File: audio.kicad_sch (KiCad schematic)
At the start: 15 parts, among them SW1 SW_DPST

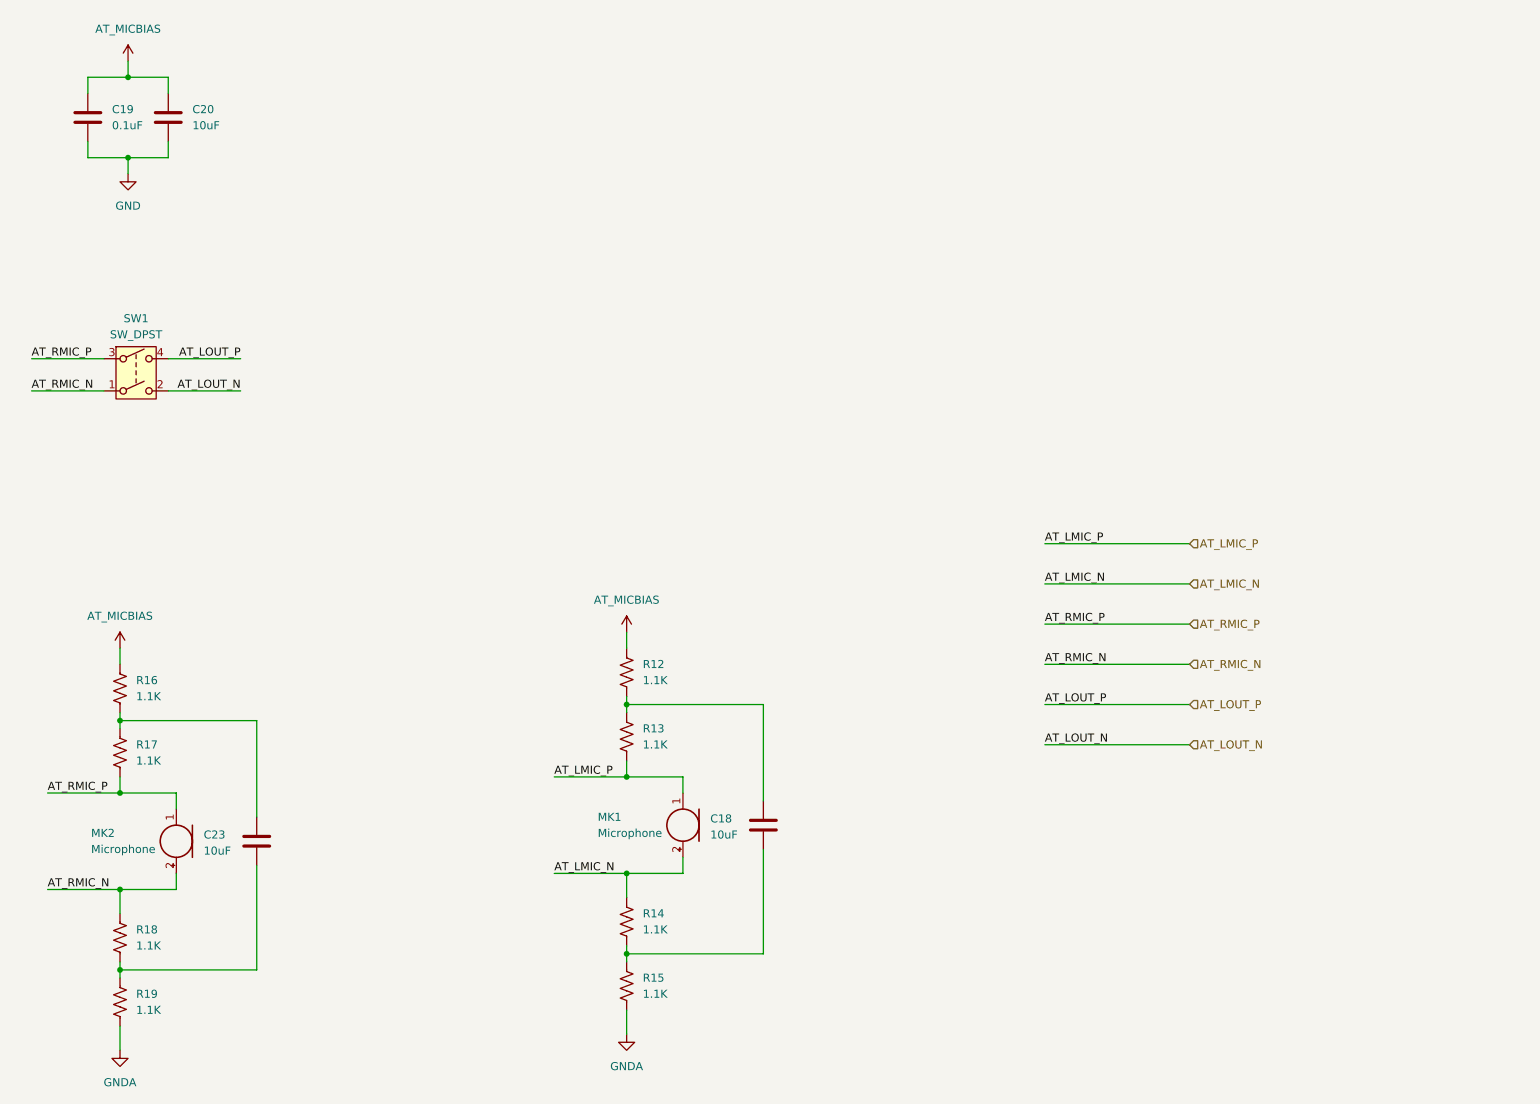
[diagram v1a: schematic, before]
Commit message: fix at820 sym, impl audio pa
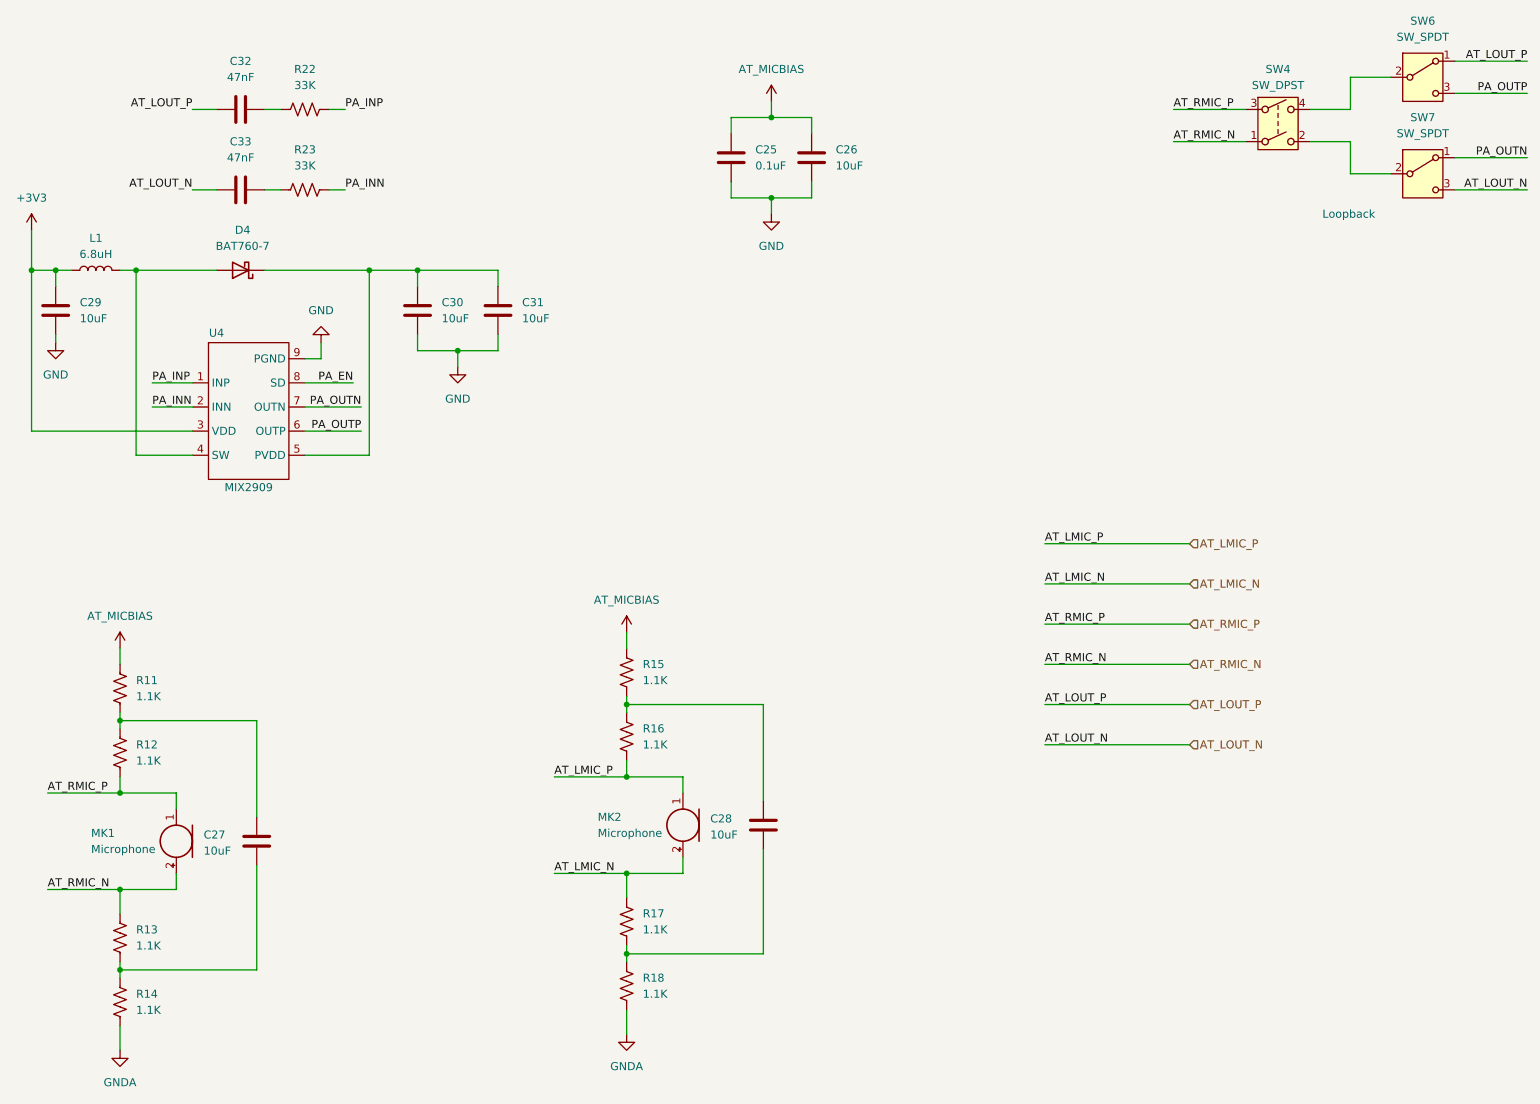
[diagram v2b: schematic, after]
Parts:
- added C29, C30, C31: 10uF, symbol Device:C
- added C32, C33: 47nF, symbol Device:C
- added D4: BAT760-7, Diode_SMD:D_SOD-323, symbol Diode:BAT60A
- added L1: 6.8uH, symbol Device:L
- added R22, R23: 33K, symbol Device:R_US
- added SW6, SW7: SW_SPDT, Button_Switch_SMD:Nidec_Copal_CAS-120A, symbol Switch:SW_SPDT
- added U4: MIX2909, Package_SO:SOIC-8-1EP_3.9x4.9mm_P1.27mm_EP2.29x3mm_ThermalVias, symbol audio:MIX2909
- renumbered C19 to C25, C20 to C26, C23 to C27, C18 to C28, MK2 to MK1, MK1 to MK2, R16 to R11, R17 to R12, R18 to R13, R19 to R14, R12 to R15, R13 to R16, R14 to R17, R15 to R18, SW1 to SW4
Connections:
- net AT_LOUT_N: now also C33.1, SW7.3 (C); no longer SW4.2
- net AT_LOUT_P: now also C32.1, SW6.1 (A); no longer SW4.4
- net GND: now also C29.2, C30.2, C31.2, U4.9 (PGND)
- new net: D4.2 (A), L1.2, U4.4 (SW)
- new net: C32.2, R22.1
- new net: C30.1, C31.1, D4.1 (K), U4.5 (PVDD)
- new net: SW4.2, SW7.2 (B)
- new net: SW4.4, SW6.2 (B)
- new net: C33.2, R23.1
- new net +3V3: C29.1, L1.1, U4.3 (VDD)
- new net PA_EN: U4.8 (SD)
- new net PA_INN: R23.2, U4.2 (INN)
- new net PA_INP: R22.2, U4.1 (INP)
- new net PA_OUTN: SW7.1 (A), U4.7 (OUTN)
- new net PA_OUTP: SW6.3 (C), U4.6 (OUTP)
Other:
- note added: "Loopback"
- moved on the sheet: C25, C26, SW4

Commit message: sch features done, all drc passed
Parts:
- renumbered C29 to C27, C32 to C28, C33 to C29, C27 to C30, C30 to C31, C31 to C32, C25 to C33, C28 to C34, C26 to C35, R11 to R14, R12 to R15, R13 to R16, R14 to R17, R22 to R18, R23 to R19, R15 to R20, R16 to R21, R17 to R22, R18 to R23, SW4 to SW6, SW6 to SW7, SW7 to SW8
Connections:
- net +3V3 renamed +5V

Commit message: asigning footprint
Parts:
- C27, C28, C29, C30, C31, C32, C33, C34, C35: footprint (none) -> Capacitor_SMD:C_0603_1608Metric_Pad1.08x0.95mm_HandSolder
- D4: footprint Diode_SMD:D_SOD-323 -> Diode_SMD:D_SOD-323_HandSoldering
- L1: footprint (none) -> Inductor_SMD:L_0603_1608Metric_Pad1.05x0.95mm_HandSolder
- R14, R15, R16, R17, R18, R19, R20, R21, R22, R23: footprint (none) -> Resistor_SMD:R_0603_1608Metric_Pad0.98x0.95mm_HandSolder
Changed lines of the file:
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@@
 			)
 		)
-		(property "Footprint" ""
+		(property "Footprint" "Capacitor_SMD:C_0603_1608Metric_Pad1.08x0.95mm_HandSolder"
 			(at 141.9352 46.99 0)
 			(hide yes)
@@
 			)
 		)
-		(property "Footprint" ""
+		(property "Footprint" "Capacitor_SMD:C_0603_1608Metric_Pad1.08x0.95mm_HandSolder"
 			(at 35.2552 71.12 0)
 			(hide yes)
@@
 			)
 		)
-		(property "Footprint" ""
+		(property "Footprint" "Resistor_SMD:R_0603_1608Metric_Pad0.98x0.95mm_HandSolder"
 			(at 125.476 174.244 90)
 			(hide yes)
@@
 			)
 		)
-		(property "Footprint" ""
+		(property "Footprint" "Inductor_SMD:L_0603_1608Metric_Pad1.05x0.95mm_HandSolder"
 			(at 40.64 60.96 0)
 			(hide yes)
@@
 			)
 		)
-		(property "Footprint" ""
+		(property "Footprint" "Resistor_SMD:R_0603_1608Metric_Pad0.98x0.95mm_HandSolder"
 			(at 73.914 34.544 90)
 			(hide yes)
@@
 			)
 		)
-		(property "Footprint" ""
+		(property "Footprint" "Capacitor_SMD:C_0603_1608Metric_Pad1.08x0.95mm_HandSolder"
 			(at 92.4052 71.12 0)
 			(hide yes)
@@
 			)
 		)
-		(property "Footprint" ""
+		(property "Footprint" "Resistor_SMD:R_0603_1608Metric_Pad0.98x0.95mm_HandSolder"
 			(at 45.466 176.784 90)
 			(hide yes)
@@
 			)
 		)
-		(property "Footprint" ""
+		(property "Footprint" "Resistor_SMD:R_0603_1608Metric_Pad0.98x0.95mm_HandSolder"
 			(at 45.466 127.254 90)
 			(hide yes)
@@
 			)
 		)
-		(property "Footprint" ""
+		(property "Footprint" "Resistor_SMD:R_0603_1608Metric_Pad0.98x0.95mm_HandSolder"
 			(at 45.466 137.414 90)
 			(hide yes)
@@
 			)
 		)
-		(property "Footprint" "Diode_SMD:D_SOD-323"
+		(property "Footprint" "Diode_SMD:D_SOD-323_HandSoldering"
 			(at 63.5 56.515 0)
 			(hide yes)
@@
 			)
 		)
-		(property "Footprint" ""
+		(property "Footprint" "Capacitor_SMD:C_0603_1608Metric_Pad1.08x0.95mm_HandSolder"
 			(at 145.0848 144.78 0)
 			(hide yes)
@@
 			)
 		)
-		(property "Footprint" ""
+		(property "Footprint" "Resistor_SMD:R_0603_1608Metric_Pad0.98x0.95mm_HandSolder"
 			(at 125.476 124.714 90)
 			(hide yes)
@@
 			)
 		)
-		(property "Footprint" ""
+		(property "Footprint" "Capacitor_SMD:C_0603_1608Metric_Pad1.08x0.95mm_HandSolder"
 			(at 65.0748 147.32 0)
 			(hide yes)
@@
 			)
 		)
-		(property "Footprint" ""
+		(property "Footprint" "Capacitor_SMD:C_0603_1608Metric_Pad1.08x0.95mm_HandSolder"
 			(at 67.31 47.2948 0)
 			(hide yes)
@@
 			)
 		)
-		(property "Footprint" ""
+		(property "Footprint" "Capacitor_SMD:C_0603_1608Metric_Pad1.08x0.95mm_HandSolder"
 			(at 154.6352 46.99 0)
 			(hide yes)
@@
 			)
 		)
-		(property "Footprint" ""
+		(property "Footprint" "Capacitor_SMD:C_0603_1608Metric_Pad1.08x0.95mm_HandSolder"
 			(at 105.1052 71.12 0)
 			(hide yes)
@@
 			)
 		)
-		(property "Footprint" ""
+		(property "Footprint" "Capacitor_SMD:C_0603_1608Metric_Pad1.08x0.95mm_HandSolder"
 			(at 67.31 34.5948 0)
 			(hide yes)
@@
 			)
 		)
-		(property "Footprint" ""
+		(property "Footprint" "Resistor_SMD:R_0603_1608Metric_Pad0.98x0.95mm_HandSolder"
 			(at 125.476 164.084 90)
 			(hide yes)
@@
 			)
 		)
-		(property "Footprint" ""
+		(property "Footprint" "Resistor_SMD:R_0603_1608Metric_Pad0.98x0.95mm_HandSolder"
 			(at 73.914 47.244 90)
 			(hide yes)
@@
 			)
 		)
-		(property "Footprint" ""
+		(property "Footprint" "Resistor_SMD:R_0603_1608Metric_Pad0.98x0.95mm_HandSolder"
 			(at 125.476 134.874 90)
 			(hide yes)
@@
 			)
 		)
-		(property "Footprint" ""
+		(property "Footprint" "Resistor_SMD:R_0603_1608Metric_Pad0.98x0.95mm_HandSolder"
 			(at 45.466 166.624 90)
 			(hide yes)

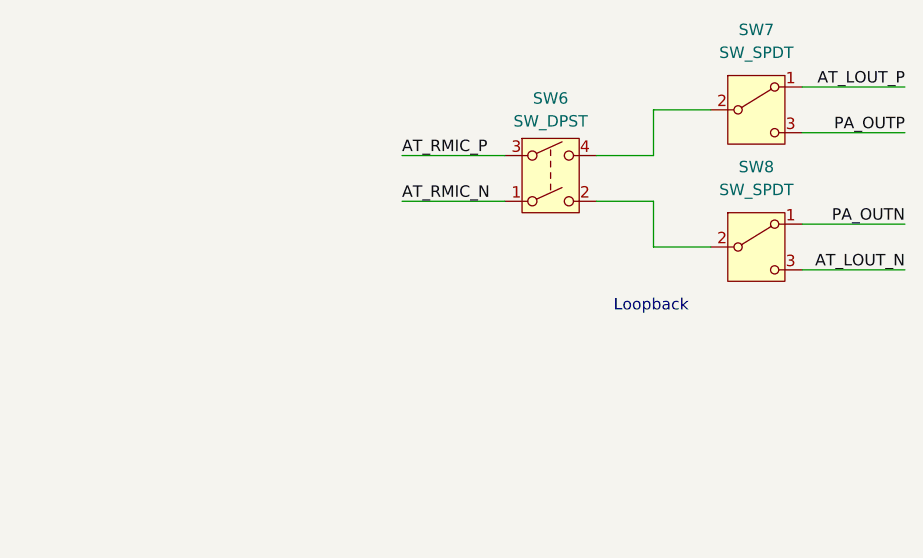
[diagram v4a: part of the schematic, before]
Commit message: refactor some switch circuit
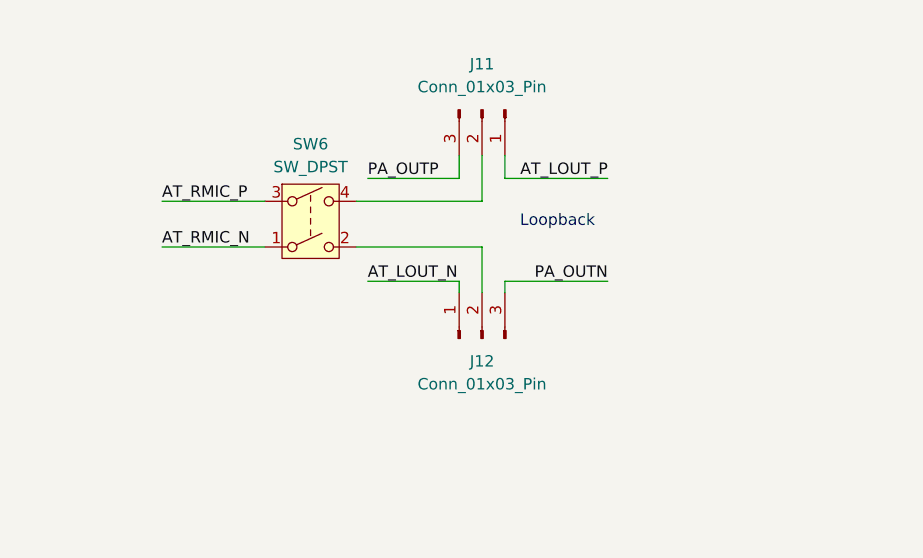
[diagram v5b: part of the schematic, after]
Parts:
- removed SW7, SW8: SW_SPDT, Button_Switch_SMD:Nidec_Copal_CAS-120A, symbol Switch:SW_SPDT
- added J11, J12: Conn_01x03_Pin, Connector_PinHeader_2.54mm:PinHeader_1x03_P2.54mm_Vertical, symbol Connector:Conn_01x03_Pin
- MK1, MK2: footprint (none) -> Capacitor_THT:CP_Radial_D4.0mm_P1.50mm
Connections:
- net AT_LOUT_N: now also J12.1 (Pin_1)
- net AT_LOUT_P: now also J11.1 (Pin_1)
- net PA_OUTN: now also J12.3 (Pin_3)
- net PA_OUTP: now also J11.3 (Pin_3)
- net at SW6.2: now also J12.2 (Pin_2)
- net at SW6.4: now also J11.2 (Pin_2)
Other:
- moved on the sheet: SW6

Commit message: sch all done, footprint done
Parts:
- added LS1: Speaker, Connector_Molex:Molex_PicoBlade_53047-0210_1x02_P1.25mm_Vertical, symbol Device:Speaker
- C28, C29: value 47nF -> 0.1uF
- D4: value BAT760-7 -> SS14; footprint Diode_SMD:D_SOD-323_HandSoldering -> Diode_SMD:D_SMA-SMB_Universal_Handsoldering
- L1: footprint Inductor_SMD:L_0603_1608Metric_Pad1.05x0.95mm_HandSolder -> Inductor_SMD:L_Sunlord_MWSA0402S
- R19: renamed from R18; value 33K -> 39K
- R20: renamed from R19; value 33K -> 39K
- SW5: renamed from SW6; footprint (none) -> Connector_PinHeader_2.54mm:PinHeader_2x02_P2.54mm_Vertical
- renumbered R14 to R15, R15 to R16, R16 to R17, R17 to R18, R20 to R21, R21 to R22, R22 to R23, R23 to R24, U4 to U5
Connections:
- net PA_OUTN: now also LS1.2
- net PA_OUTP: now also LS1.1

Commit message: components loc done, pcb ing
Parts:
- SW5: footprint Connector_PinHeader_2.54mm:PinHeader_2x02_P2.54mm_Vertical -> Button_Switch_SMD:SW_DIP_SPSTx02_Slide_Copal_CHS-02B_W7.62mm_P1.27mm
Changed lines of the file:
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@@
 			)
 		)
-		(property "Footprint" "Connector_PinHeader_2.54mm:PinHeader_2x02_P2.54mm_Vertical"
+		(property "Footprint" "Button_Switch_SMD:SW_DIP_SPSTx02_Slide_Copal_CHS-02B_W7.62mm_P1.27mm"
 			(at 200.66 43.18 0)
 			(hide yes)
